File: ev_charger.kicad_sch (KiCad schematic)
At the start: 33 parts, among them J1 Conn_01x03, J2 Conn_01x02, J3 Conn_01x02, J4 Conn_01x04, J5 Conn_01x02, J6 Conn_01x02, J7 Conn_01x02, J8 Conn_01x02, J9 Conn_01x02, U1 TPS61040DBV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

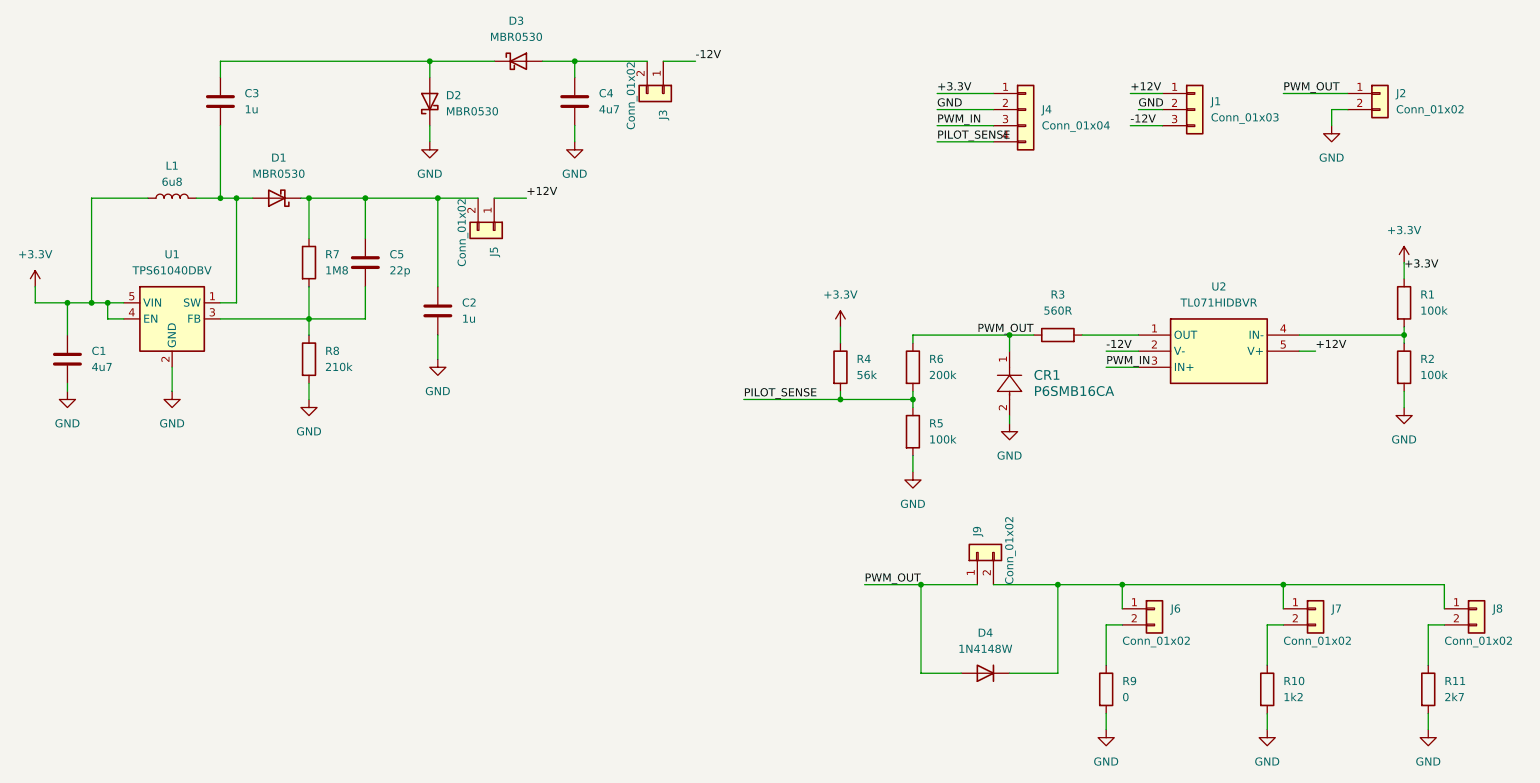
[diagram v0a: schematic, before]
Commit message: Adjust resistor values
- Change r3 to 1k to adjust output CE PWM voltage.
- Change r4 to 46k to increase bias. This avoids negative sense
  voltages.
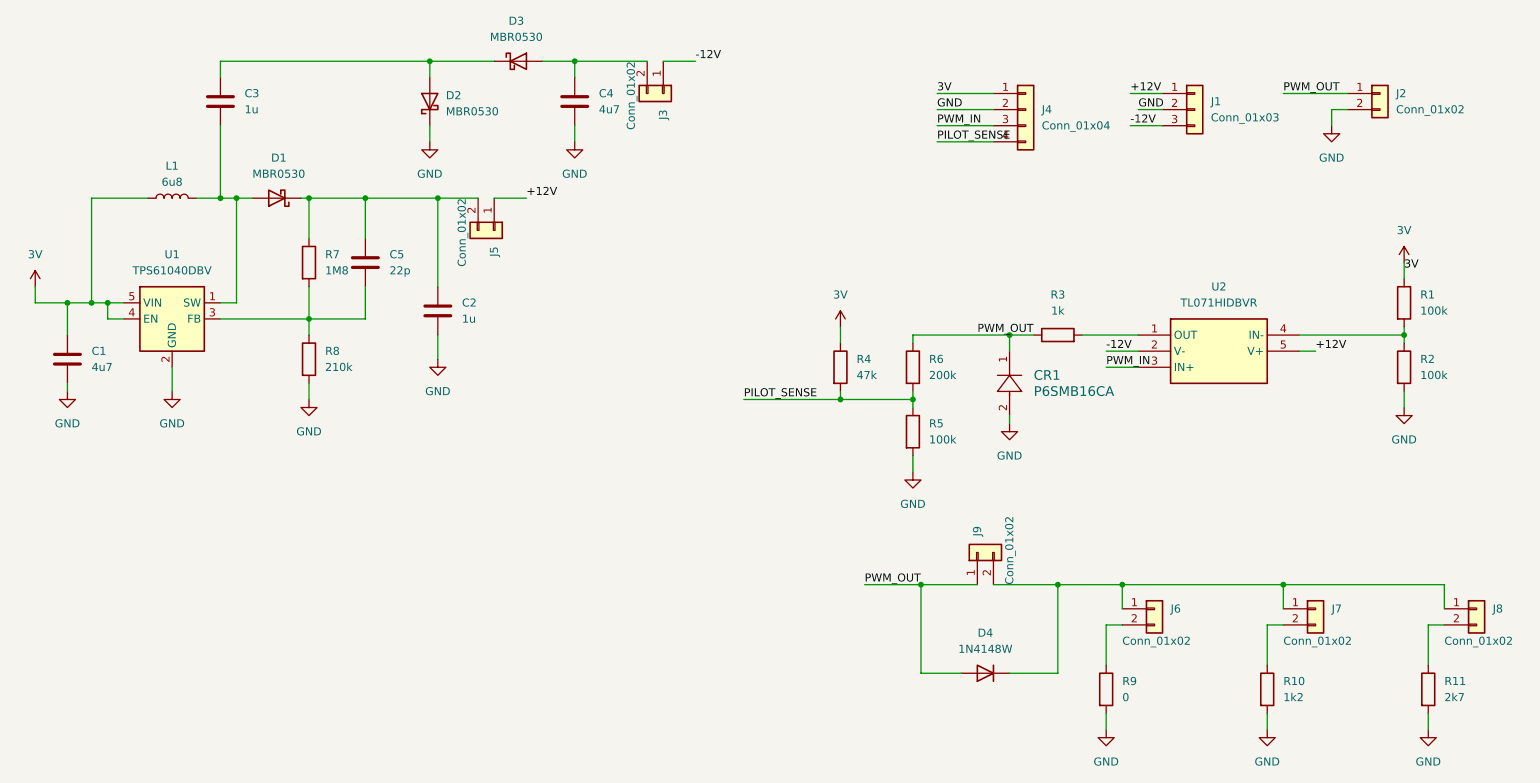
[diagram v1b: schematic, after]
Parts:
- R3: value 560R -> 1k; LCSC C23204 -> C21190
- R4: value 56k -> 47k; LCSC C23206 -> C25819
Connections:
- net +3.3V renamed 3V
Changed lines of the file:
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@@
 		)
 	)
-	(label "+3.3V"
+	(label "3V"
 		(at 234.95 58.42 0)
 		(effects
@@
 		)
 	)
-	(label "+3.3V"
+	(label "3V"
 		(at 161.29 30.48 0)
 		(effects
@@
 			)
 		)
-		(property "Value" "+3.3V"
+		(property "Value" "3V"
 			(at 19.05 55.88 0)
 			(effects
@@
 			)
 		)
-		(property "Value" "+3.3V"
+		(property "Value" "3V"
 			(at 146.05 62.23 0)
 			(effects
@@
 			)
 		)
-		(property "Value" "+3.3V"
+		(property "Value" "3V"
 			(at 234.95 52.07 0)
 			(effects
@@
 			)
 		)
-		(property "Value" "56k"
+		(property "Value" "47k"
 			(at 148.59 74.9299 0)
 			(effects
@@
 			)
 		)
-		(property "LCSC" "C23206"
+		(property "LCSC" "C25819"
 			(at 146.05 73.66 0)
 			(effects
@@
 			)
 		)
-		(property "Value" "560R"
+		(property "Value" "1k"
 			(at 180.34 64.77 90)
 			(effects
@@
 			)
 		)
-		(property "LCSC" "C23204"
+		(property "LCSC" "C21190"
 			(at 180.34 68.58 90)
 			(effects
